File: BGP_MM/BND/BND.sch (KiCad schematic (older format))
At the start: 5 parts, among them J1 Conn_01x02, J2 Conn_01x03, P1 CONN_01X04, P2 Conn_01x02

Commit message: MM Routing complete
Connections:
- net Earth: now also J2.1 (Pin_1); no longer J2.3 (Pin_3)
- net VCC: now also J1.2 (Pin_2); no longer J1.1 (Pin_1)
- new net: J1.1 (Pin_1), J2.3 (Pin_3)
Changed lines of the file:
@@
 L Conn_01x02 J1
 U 1 1 5AE4EB86
-P 6650 3450
-F 0 "J1" H 6650 3550 50  0000 C CNN
-F 1 "Conn_01x02" H 6650 3250 50  0001 C CNN
-F 2 "Terminal_Blocks:TerminalBlock_Pheonix_MPT-2.54mm_2pol" H 6650 3450 50  0001 C CNN
-F 3 "" H 6650 3450 50  0001 C CNN
-	1    6650 3450
-	-1   0    0    -1
+P 6650 3550
+F 0 "J1" H 6650 3650 50  0000 C CNN
+F 1 "Conn_01x02" H 6650 3350 50  0001 C CNN
+F 2 "Terminal_Blocks:TerminalBlock_Pheonix_MPT-2.54mm_2pol" H 6650 3550 50  0001 C CNN
+F 3 "" H 6650 3550 50  0001 C CNN
+	1    6650 3550
+	-1   0    0    1
 $EndComp
 $Comp
@@
 F 3 "" H 6650 3850 50  0001 C CNN
 	1    6650 3850
-	-1   0    0    -1
+	-1   0    0    1
 $EndComp
 $Comp

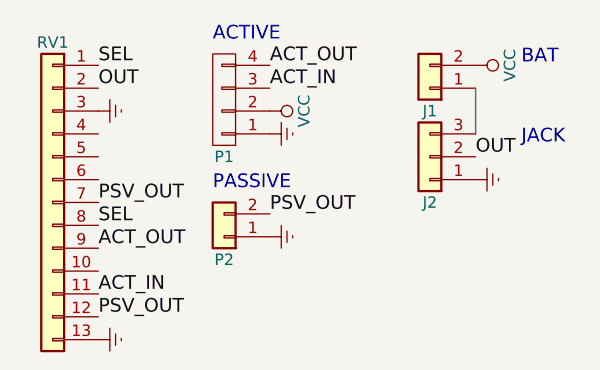
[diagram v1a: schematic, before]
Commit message: MM Connector Verification
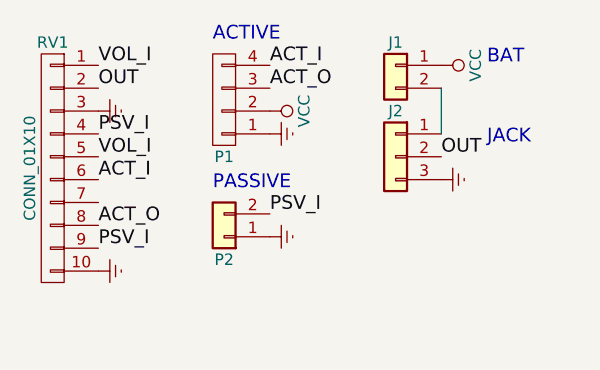
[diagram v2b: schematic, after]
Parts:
- removed RV1: Conn_01x13, LIBS:Bournes_Blend_PP, symbol Conn_01x13
- added RV1: CONN_01X10, LIBS:Bournes_Blend_PP_PCB, symbol CONN_01X10
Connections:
- net Earth: now also J2.3 (Pin_3), RV1.10 (P10), RV1.3 (P3); no longer J2.1 (Pin_1)
- net OUT: now also RV1.2 (P2)
- net VCC: now also J1.1 (Pin_1); no longer J1.2 (Pin_2)
- net ACT_IN renamed ACT_O
- net ACT_O: now also RV1.8 (P8)
- net ACT_OUT renamed ACT_I
- net ACT_I: now also RV1.6 (P6)
- net PSV_OUT renamed PSV_I
- net PSV_I: now also RV1.4 (P4), RV1.9 (P9)
- new net: J1.2 (Pin_2), J2.1 (Pin_1)
- new net VOL_I: RV1.1 (P1), RV1.5 (P5)
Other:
- moved on the sheet: J1, J2
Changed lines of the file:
@@
 $EndDescr
-$Comp
-L Conn_01x13 RV1
-U 1 1 5AE4EAE8
-P 5000 4050
-F 0 "RV1" H 5000 4750 50  0000 C CNN
-F 1 "Conn_01x13" H 5000 3350 50  0001 C CNN
-F 2 "LIBS:Bournes_Blend_PP" H 5000 4050 50  0001 C CNN
-F 3 "" H 5000 4050 50  0001 C CNN
-	1    5000 4050
-	-1   0    0    -1
-$EndComp
 $Comp
 L Conn_01x02 J1
 U 1 1 5AE4EB86
-P 6650 3550
-F 0 "J1" H 6650 3650 50  0000 C CNN
-F 1 "Conn_01x02" H 6650 3350 50  0001 C CNN
-F 2 "Terminal_Blocks:TerminalBlock_Pheonix_MPT-2.54mm_2pol" H 6650 3550 50  0001 C CNN
-F 3 "" H 6650 3550 50  0001 C CNN
-	1    6650 3550
-	-1   0    0    1
+P 6500 3450
+F 0 "J1" H 6500 3550 50  0000 C CNN
+F 1 "Conn_01x02" H 6500 3250 50  0001 C CNN
+F 2 "Terminal_Blocks:TerminalBlock_Pheonix_MPT-2.54mm_2pol" H 6500 3450 50  0001 C CNN
+F 3 "" H 6500 3450 50  0001 C CNN
+	1    6500 3450
+	-1   0    0    -1
 $EndComp
 $Comp
 L Earth #PWR01
 U 1 1 5AE4ECAD
-P 5200 4650
-F 0 "#PWR01" H 5200 4400 50  0001 C CNN
-F 1 "Earth" H 5200 4500 50  0001 C CNN
-F 2 "" H 5200 4650 50  0001 C CNN
-F 3 "" H 5200 4650 50  0001 C CNN
-	1    5200 4650
+P 5200 4350
+F 0 "#PWR01" H 5200 4100 50  0001 C CNN
+F 1 "Earth" H 5200 4200 50  0001 C CNN
+F 2 "" H 5200 4350 50  0001 C CNN
+F 3 "" H 5200 4350 50  0001 C CNN
+	1    5200 4350
 	0    -1   -1   0
 $EndComp
@@
 L Conn_01x03 J2
 U 1 1 5AE533B1
-P 6650 3850
-F 0 "J2" H 6650 4050 50  0000 C CNN
-F 1 "Conn_01x03" H 6650 3650 50  0001 C CNN
-F 2 "Terminal_Blocks:TerminalBlock_Pheonix_MPT-2.54mm_3pol" H 6650 3850 50  0001 C CNN
-F 3 "" H 6650 3850 50  0001 C CNN
-	1    6650 3850
-	-1   0    0    1
+P 6500 3850
+F 0 "J2" H 6500 4050 50  0000 C CNN
+F 1 "Conn_01x03" H 6500 3650 50  0001 C CNN
+F 2 "Terminal_Blocks:TerminalBlock_Pheonix_MPT-2.54mm_3pol" H 6500 3850 50  0001 C CNN
+F 3 "" H 6500 3850 50  0001 C CNN
+	1    6500 3850
+	-1   0    0    -1
 $EndComp
 $Comp
@@
 L Earth #PWR04
 U 1 1 5B063927
-P 6850 3950
-F 0 "#PWR04" H 6850 3700 50  0001 C CNN
-F 1 "Earth" H 6850 3800 50  0001 C CNN
-F 2 "" H 6850 3950 50  0001 C CNN
-F 3 "" H 6850 3950 50  0001 C CNN
-	1    6850 3950
+P 6700 3950
+F 0 "#PWR04" H 6700 3700 50  0001 C CNN
+F 1 "Earth" H 6700 3800 50  0001 C CNN
+F 2 "" H 6700 3950 50  0001 C CNN
+F 3 "" H 6700 3950 50  0001 C CNN
+	1    6700 3950
 	0    -1   -1   0
 $EndComp
-Text Label 6850 3850 0    60   ~ 0
+Text Label 6700 3850 0    60   ~ 0
 OUT
-Wire Wire Line
-	6850 3750 6850 3550
 $Comp
 L VCC #PWR05
 U 1 1 5B063954
-P 6850 3450
-F 0 "#PWR05" H 6850 3300 50  0001 C CNN
-F 1 "VCC" H 6850 3600 50  0000 C CNN
-F 2 "" H 6850 3450 50  0000 C CNN
-F 3 "" H 6850 3450 50  0000 C CNN
-	1    6850 3450
+P 6700 3450
+F 0 "#PWR05" H 6700 3300 50  0001 C CNN
+F 1 "VCC" H 6700 3600 50  0000 C CNN
+F 2 "" H 6700 3450 50  0000 C CNN
+F 3 "" H 6700 3450 50  0000 C CNN
+	1    6700 3450
 	0    1    1    0
 $EndComp
 Text Label 5950 3550 0    60   ~ 0
-ACT_IN
+ACT_O
 Text Label 5950 3450 0    60   ~ 0
-ACT_OUT
-Text Notes 7050 3450 0    60   ~ 0
+ACT_I
+Text Notes 6900 3450 0    60   ~ 0
 BAT
-Text Notes 7050 3800 0    60   ~ 0
+Text Notes 6900 3800 0    60   ~ 0
 JACK
 Text Notes 5700 3350 0    60   ~ 0
@@
 $EndComp
 Text Label 5950 4100 0    60   ~ 0
-PSV_OUT
+PSV_I
 Text Label 5200 3550 0    60   ~ 0
 OUT
-Text Label 5200 4150 0    60   ~ 0
-SEL
 Text Label 5200 3450 0    60   ~ 0
-SEL
+VOL_I
 $Comp
 L Earth #PWR07
@@
 	0    -1   -1   0
 $EndComp
-Text Label 5200 4050 0    60   ~ 0
-PSV_OUT
+Text Label 5200 3750 0    60   ~ 0
+PSV_I
+Text Label 5200 3950 0    60   ~ 0
+ACT_I
+Text Label 5200 4150 0    60   ~ 0
+ACT_O
 Text Label 5200 4250 0    60   ~ 0
-ACT_OUT
-Text Label 5200 4450 0    60   ~ 0
-ACT_IN
-Text Label 5200 4550 0    60   ~ 0
-PSV_OUT
+PSV_I
+Text Label 5200 3850 0    60   ~ 0
+VOL_I
+Wire Wire Line
+	6700 3750 6700 3550
+$Comp
+L CONN_01X10 RV1
+U 1 1 5B0F69E0
+P 5000 3900
+F 0 "RV1" H 5000 4450 50  0000 C CNN
+F 1 "CONN_01X10" V 5100 3900 50  0000 C CNN
+F 2 "LIBS:Bournes_Blend_PP_PCB" H 5000 3900 50  0001 C CNN
+F 3 "" H 5000 3900 50  0000 C CNN
+	1    5000 3900
+	-1   0    0    -1
+$EndComp
 $EndSCHEMATC

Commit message: MM Refactoring
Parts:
- removed P1: CONN_01X04, Connectors_JST:JST_PH_B4B-PH-K_04x2.00mm_Straight, symbol CONN_01X04
- removed P2: Conn_01x02, Connectors_JST:JST_PH_B2B-PH-K_02x2.00mm_Straight, symbol Conn_01x02
- removed RV1: CONN_01X10, LIBS:Bournes_Blend_PP_PCB, symbol CONN_01X10
- added P1: CONN_01X02, Connectors_JST:JST_PH_B2B-PH-K_02x2.00mm_Straight, symbol CONN_01X02
- added RV1: POT, LIBS:Potentiometer_Alpha_RV16, symbol POT
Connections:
- net Earth: now also P1.1 (P1)
- net OUT: now also RV1.1
- new net: P1.2 (P2), RV1.2
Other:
- note removed: "ACTIVE"
- note removed: "PASSIVE"
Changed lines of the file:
@@
-$EndComp
-$Comp
-L Earth #PWR01
-U 1 1 5AE4ECAD
-P 5200 4350
-F 0 "#PWR01" H 5200 4100 50  0001 C CNN
-F 1 "Earth" H 5200 4200 50  0001 C CNN
-F 2 "" H 5200 4350 50  0001 C CNN
-F 3 "" H 5200 4350 50  0001 C CNN
-	1    5200 4350
-	0    -1   -1   0
 $EndComp
 $Comp
@@
 $EndComp
 $Comp
-L CONN_01X04 P1
-U 1 1 5B0637E4
-P 5750 3600
-F 0 "P1" H 5750 3850 50  0000 C CNN
-F 1 "CONN_01X04" V 5850 3600 50  0001 C CNN
-F 2 "Connectors_JST:JST_PH_B4B-PH-K_04x2.00mm_Straight" H 5750 3600 50  0001 C CNN
-F 3 "" H 5750 3600 50  0000 C CNN
-	1    5750 3600
-	-1   0    0    1
-$EndComp
-$Comp
-L Earth #PWR02
-U 1 1 5B0638D5
-P 5950 3750
-F 0 "#PWR02" H 5950 3500 50  0001 C CNN
-F 1 "Earth" H 5950 3600 50  0001 C CNN
-F 2 "" H 5950 3750 50  0001 C CNN
-F 3 "" H 5950 3750 50  0001 C CNN
-	1    5950 3750
-	0    -1   -1   0
-$EndComp
-$Comp
-L VCC #PWR03
-U 1 1 5B0638EA
-P 5950 3650
-F 0 "#PWR03" H 5950 3500 50  0001 C CNN
-F 1 "VCC" H 5950 3800 50  0000 C CNN
-F 2 "" H 5950 3650 50  0000 C CNN
-F 3 "" H 5950 3650 50  0000 C CNN
-	1    5950 3650
-	0    1    1    0
-$EndComp
-$Comp
-L Earth #PWR04
+L Earth #PWR01
 U 1 1 5B063927
 P 6700 3950
-F 0 "#PWR04" H 6700 3700 50  0001 C CNN
+F 0 "#PWR01" H 6700 3700 50  0001 C CNN
 F 1 "Earth" H 6700 3800 50  0001 C CNN
 F 2 "" H 6700 3950 50  0001 C CNN
@@
 OUT
 $Comp
-L VCC #PWR05
+L VCC #PWR02
 U 1 1 5B063954
 P 6700 3450
-F 0 "#PWR05" H 6700 3300 50  0001 C CNN
+F 0 "#PWR02" H 6700 3300 50  0001 C CNN
 F 1 "VCC" H 6700 3600 50  0000 C CNN
 F 2 "" H 6700 3450 50  0000 C CNN
@@
 	0    1    1    0
 $EndComp
-Text Label 5950 3550 0    60   ~ 0
-ACT_O
-Text Label 5950 3450 0    60   ~ 0
-ACT_I
 Text Notes 6900 3450 0    60   ~ 0
 BAT
 Text Notes 6900 3800 0    60   ~ 0
 JACK
-Text Notes 5700 3350 0    60   ~ 0
-ACTIVE
-Text Notes 5700 4000 0    60   ~ 0
-PASSIVE
-$Comp
-L Conn_01x02 P2
-U 1 1 5B063ABD
-P 5750 4200
-F 0 "P2" H 5750 4300 50  0000 C CNN
-F 1 "Conn_01x02" H 5750 4000 50  0001 C CNN
-F 2 "Connectors_JST:JST_PH_B2B-PH-K_02x2.00mm_Straight" H 5750 4200 50  0001 C CNN
-F 3 "" H 5750 4200 50  0001 C CNN
-	1    5750 4200
-	-1   0    0    1
-$EndComp
-$Comp
-L Earth #PWR06
-U 1 1 5B063B7B
-P 5950 4200
-F 0 "#PWR06" H 5950 3950 50  0001 C CNN
-F 1 "Earth" H 5950 4050 50  0001 C CNN
-F 2 "" H 5950 4200 50  0001 C CNN
-F 3 "" H 5950 4200 50  0001 C CNN
-	1    5950 4200
-	0    -1   -1   0
-$EndComp
-Text Label 5950 4100 0    60   ~ 0
-PSV_I
-Text Label 5200 3550 0    60   ~ 0
-OUT
-Text Label 5200 3450 0    60   ~ 0
-VOL_I
-$Comp
-L Earth #PWR07
-U 1 1 5B063C07
-P 5200 3650
-F 0 "#PWR07" H 5200 3400 50  0001 C CNN
-F 1 "Earth" H 5200 3500 50  0001 C CNN
-F 2 "" H 5200 3650 50  0001 C CNN
-F 3 "" H 5200 3650 50  0001 C CNN
-	1    5200 3650
-	0    -1   -1   0
-$EndComp
-Text Label 5200 3750 0    60   ~ 0
-PSV_I
-Text Label 5200 3950 0    60   ~ 0
-ACT_I
-Text Label 5200 4150 0    60   ~ 0
-ACT_O
-Text Label 5200 4250 0    60   ~ 0
-PSV_I
-Text Label 5200 3850 0    60   ~ 0
-VOL_I
 Wire Wire Line
 	6700 3750 6700 3550
 $Comp
-L CONN_01X10 RV1
-U 1 1 5B0F69E0
-P 5000 3900
-F 0 "RV1" H 5000 4450 50  0000 C CNN
-F 1 "CONN_01X10" V 5100 3900 50  0000 C CNN
-F 2 "LIBS:Bournes_Blend_PP_PCB" H 5000 3900 50  0001 C CNN
-F 3 "" H 5000 3900 50  0000 C CNN
-	1    5000 3900
-	-1   0    0    -1
+L CONN_01X02 P1
+U 1 1 5B19CB22
+P 6000 3500
+F 0 "P1" H 6000 3650 50  0000 C CNN
+F 1 "CONN_01X02" V 6100 3500 50  0001 C CNN
+F 2 "Connectors_JST:JST_PH_B2B-PH-K_02x2.00mm_Straight" H 6000 3500 50  0001 C CNN
+F 3 "" H 6000 3500 50  0000 C CNN
+	1    6000 3500
+	1    0    0    -1
 $EndComp
+$Comp
+L Earth #PWR03
+U 1 1 5B19CBB0
+P 5800 3450
+F 0 "#PWR03" H 5800 3200 50  0001 C CNN
+F 1 "Earth" H 5800 3300 50  0001 C CNN
+F 2 "" H 5800 3450 50  0000 C CNN
+F 3 "" H 5800 3450 50  0000 C CNN
+	1    5800 3450
+	0    1    1    0
+$EndComp
+$Comp
+L POT RV1
+U 1 1 5B19CBED
+P 5800 3850
+F 0 "RV1" H 5800 3770 50  0000 C CNN
+F 1 "POT" H 5800 3850 50  0000 C CNN
+F 2 "LIBS:Potentiometer_Alpha_RV16" H 5800 3850 50  0001 C CNN
+F 3 "" H 5800 3850 50  0000 C CNN
+	1    5800 3850
+	0    1    -1   0
+$EndComp
+Text Label 5950 3850 0    60   ~ 0
+OUT
+$Comp
+L Earth #PWR04
+U 1 1 5B19CC5B
+P 5800 4000
+F 0 "#PWR04" H 5800 3750 50  0001 C CNN
+F 1 "Earth" H 5800 3850 50  0001 C CNN
+F 2 "" H 5800 4000 50  0001 C CNN
+F 3 "" H 5800 4000 50  0001 C CNN
+	1    5800 4000
+	1    0    0    -1
+$EndComp
+Wire Wire Line
+	5800 3700 5800 3550
 $EndSCHEMATC

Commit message: MM Refactoring
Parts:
- removed J1: Conn_01x02, Terminal_Blocks:TerminalBlock_Pheonix_MPT-2.54mm_2pol, symbol Conn_01x02
- removed J2: Conn_01x03, Terminal_Blocks:TerminalBlock_Pheonix_MPT-2.54mm_3pol, symbol Conn_01x03
- removed P1: CONN_01X02, Connectors_JST:JST_PH_B2B-PH-K_02x2.00mm_Straight, symbol CONN_01X02
- added J1: Conn_01x03_Male, Pin_Headers:Pin_Header_Straight_1x03_Pitch2.54mm, symbol Conn_01x03_Male
- RV1: footprint LIBS:Potentiometer_Alpha_RV16 -> (none)
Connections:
- net Earth: now also RV1.1, J1.3 (Pin_3)
- net OUT: now also RV1.2, J1.2 (Pin_2); no longer RV1.1
- net IN: now reaches RV1.3
- net IN: now also J1.1 (Pin_1)
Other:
- note removed: "BAT"
- note removed: "JACK"
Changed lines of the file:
@@
 LIBS:switches
 LIBS:relays
+LIBS:motors
 LIBS:transistors
 LIBS:conn
@@
 $EndDescr
 $Comp
-L Conn_01x02 J1
-U 1 1 5AE4EB86
-P 6500 3450
-F 0 "J1" H 6500 3550 50  0000 C CNN
-F 1 "Conn_01x02" H 6500 3250 50  0001 C CNN
-F 2 "Terminal_Blocks:TerminalBlock_Pheonix_MPT-2.54mm_2pol" H 6500 3450 50  0001 C CNN
-F 3 "" H 6500 3450 50  0001 C CNN
-	1    6500 3450
-	-1   0    0    -1
+L POT RV1
+U 1 1 5B1AF2D3
+P 6150 3900
+F 0 "RV1" V 5975 3900 50  0000 C CNN
+F 1 "POT" V 6050 3900 50  0000 C CNN
+F 2 "" H 6150 3900 50  0001 C CNN
+F 3 "" H 6150 3900 50  0001 C CNN
+	1    6150 3900
+	1    0    0    1
 $EndComp
-$Comp
-L Conn_01x03 J2
-U 1 1 5AE533B1
-P 6500 3850
-F 0 "J2" H 6500 4050 50  0000 C CNN
-F 1 "Conn_01x03" H 6500 3650 50  0001 C CNN
-F 2 "Terminal_Blocks:TerminalBlock_Pheonix_MPT-2.54mm_3pol" H 6500 3850 50  0001 C CNN
-F 3 "" H 6500 3850 50  0001 C CNN
-	1    6500 3850
-	-1   0    0    -1
-$EndComp
+Text Label 6150 3750 1    60   ~ 0
+IN
+Text Label 6300 3900 0    60   ~ 0
+OUT
 $Comp
 L Earth #PWR01
-U 1 1 5B063927
-P 6700 3950
-F 0 "#PWR01" H 6700 3700 50  0001 C CNN
-F 1 "Earth" H 6700 3800 50  0001 C CNN
-F 2 "" H 6700 3950 50  0001 C CNN
-F 3 "" H 6700 3950 50  0001 C CNN
-	1    6700 3950
-	0    -1   -1   0
-$EndComp
-Text Label 6700 3850 0    60   ~ 0
-OUT
-$Comp
-L VCC #PWR02
-U 1 1 5B063954
-P 6700 3450
-F 0 "#PWR02" H 6700 3300 50  0001 C CNN
-F 1 "VCC" H 6700 3600 50  0000 C CNN
-F 2 "" H 6700 3450 50  0000 C CNN
-F 3 "" H 6700 3450 50  0000 C CNN
-	1    6700 3450
-	0    1    1    0
-$EndComp
-Text Notes 6900 3450 0    60   ~ 0
-BAT
-Text Notes 6900 3800 0    60   ~ 0
-JACK
-Wire Wire Line
-	6700 3750 6700 3550
-$Comp
-L CONN_01X02 P1
-U 1 1 5B19CB22
-P 6000 3500
-F 0 "P1" H 6000 3650 50  0000 C CNN
-F 1 "CONN_01X02" V 6100 3500 50  0001 C CNN
-F 2 "Connectors_JST:JST_PH_B2B-PH-K_02x2.00mm_Straight" H 6000 3500 50  0001 C CNN
-F 3 "" H 6000 3500 50  0000 C CNN
-	1    6000 3500
+U 1 1 5B1AF2FA
+P 6150 4050
+F 0 "#PWR01" H 6150 3800 50  0001 C CNN
+F 1 "Earth" H 6150 3900 50  0001 C CNN
+F 2 "" H 6150 4050 50  0001 C CNN
+F 3 "" H 6150 4050 50  0001 C CNN
+	1    6150 4050
 	1    0    0    -1
 $EndComp
 $Comp
-L Earth #PWR03
-U 1 1 5B19CBB0
-P 5800 3450
-F 0 "#PWR03" H 5800 3200 50  0001 C CNN
-F 1 "Earth" H 5800 3300 50  0001 C CNN
-F 2 "" H 5800 3450 50  0000 C CNN
-F 3 "" H 5800 3450 50  0000 C CNN
-	1    5800 3450
-	0    1    1    0
+L Conn_01x03_Male J1
+U 1 1 5B1AF310
+P 6550 3900
+F 0 "J1" H 6550 4100 50  0000 C CNN
+F 1 "Conn_01x03_Male" H 6550 3700 50  0001 C CNN
+F 2 "Pin_Headers:Pin_Header_Straight_1x03_Pitch2.54mm" H 6550 3900 50  0001 C CNN
+F 3 "" H 6550 3900 50  0001 C CNN
+	1    6550 3900
+	1    0    0    -1
 $EndComp
-$Comp
-L POT RV1
-U 1 1 5B19CBED
-P 5800 3850
-F 0 "RV1" H 5800 3770 50  0000 C CNN
-F 1 "POT" H 5800 3850 50  0000 C CNN
-F 2 "LIBS:Potentiometer_Alpha_RV16" H 5800 3850 50  0001 C CNN
-F 3 "" H 5800 3850 50  0000 C CNN
-	1    5800 3850
-	0    1    -1   0
-$EndComp
-Text Label 5950 3850 0    60   ~ 0
+Text Label 6750 3800 0    60   ~ 0
+IN
+Text Label 6750 3900 0    60   ~ 0
 OUT
 $Comp
-L Earth #PWR04
-U 1 1 5B19CC5B
-P 5800 4000
-F 0 "#PWR04" H 5800 3750 50  0001 C CNN
-F 1 "Earth" H 5800 3850 50  0001 C CNN
-F 2 "" H 5800 4000 50  0001 C CNN
-F 3 "" H 5800 4000 50  0001 C CNN
-	1    5800 4000
+L Earth #PWR02
+U 1 1 5B1AF35E
+P 6750 4000
+F 0 "#PWR02" H 6750 3750 50  0001 C CNN
+F 1 "Earth" H 6750 3850 50  0001 C CNN
+F 2 "" H 6750 4000 50  0001 C CNN
+F 3 "" H 6750 4000 50  0001 C CNN
+	1    6750 4000
 	1    0    0    -1
 $EndComp
-Wire Wire Line
-	5800 3700 5800 3550
 $EndSCHEMATC
